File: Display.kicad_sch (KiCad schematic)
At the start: 3 parts, among them U10 SA15-11SURKWA, U11 SA15-11SURKWA, U7 TLC5926

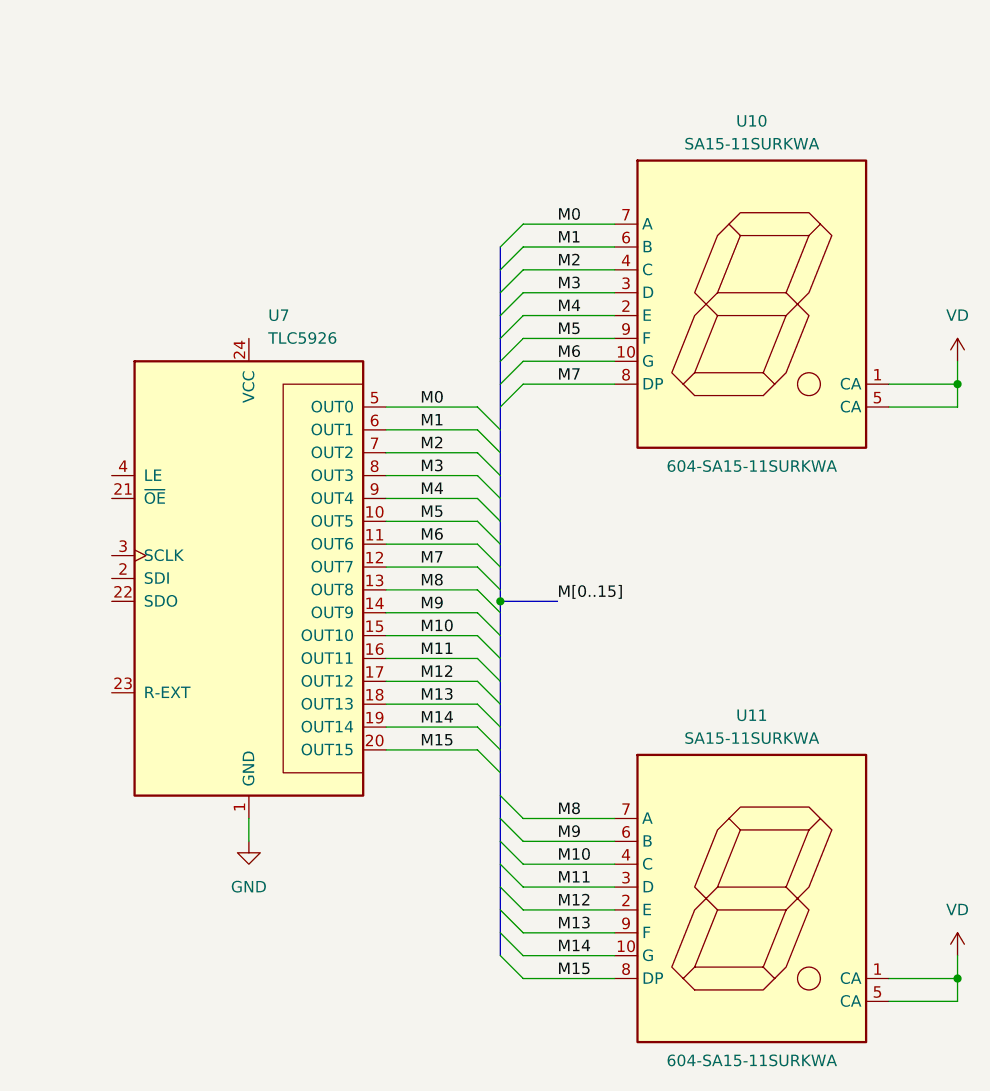
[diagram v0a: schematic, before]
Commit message: display driver update
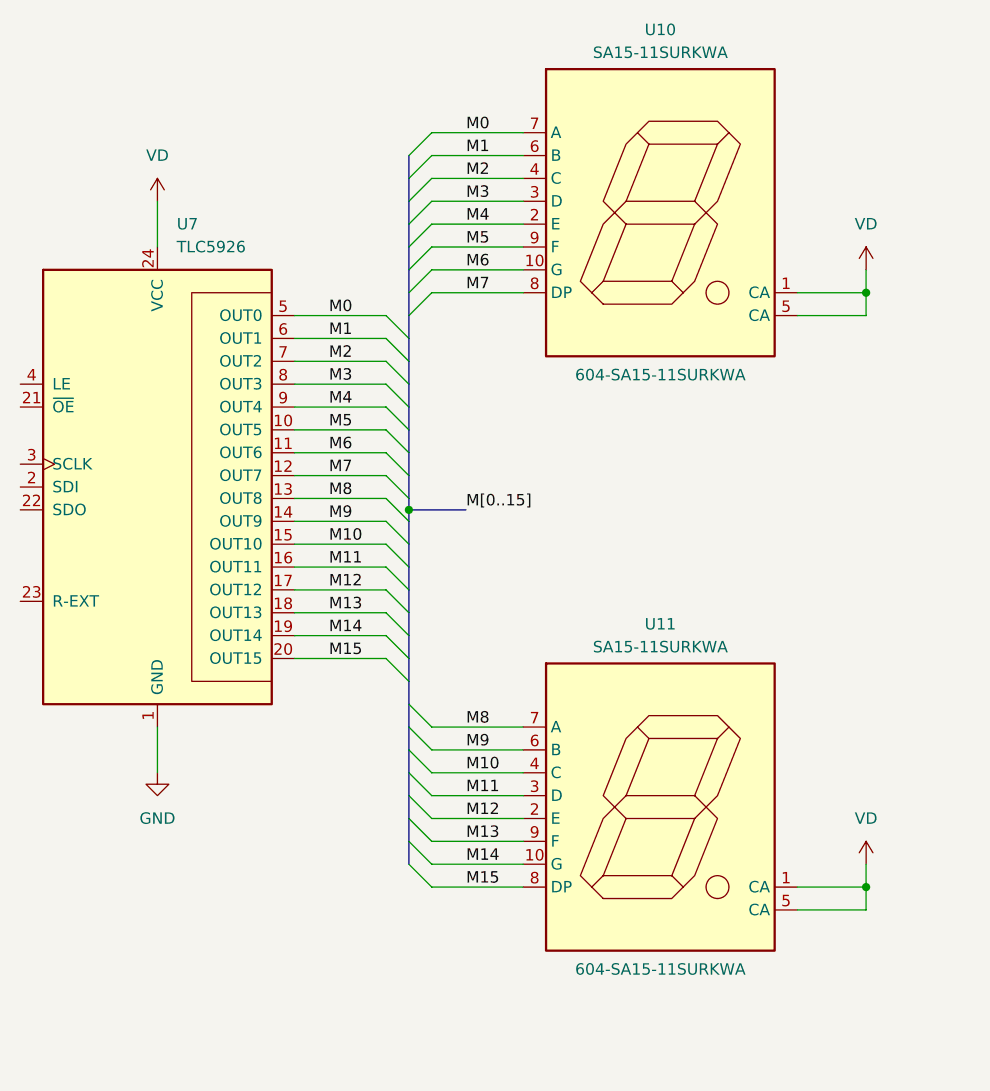
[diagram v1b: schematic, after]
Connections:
- net VD: now also U7.24 (VCC)
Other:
- moved on the sheet: U10, U11, U7
